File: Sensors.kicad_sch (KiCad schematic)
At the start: 3 parts, among them U2 ICM-42688-P, U3 BMP280, U4 INA226

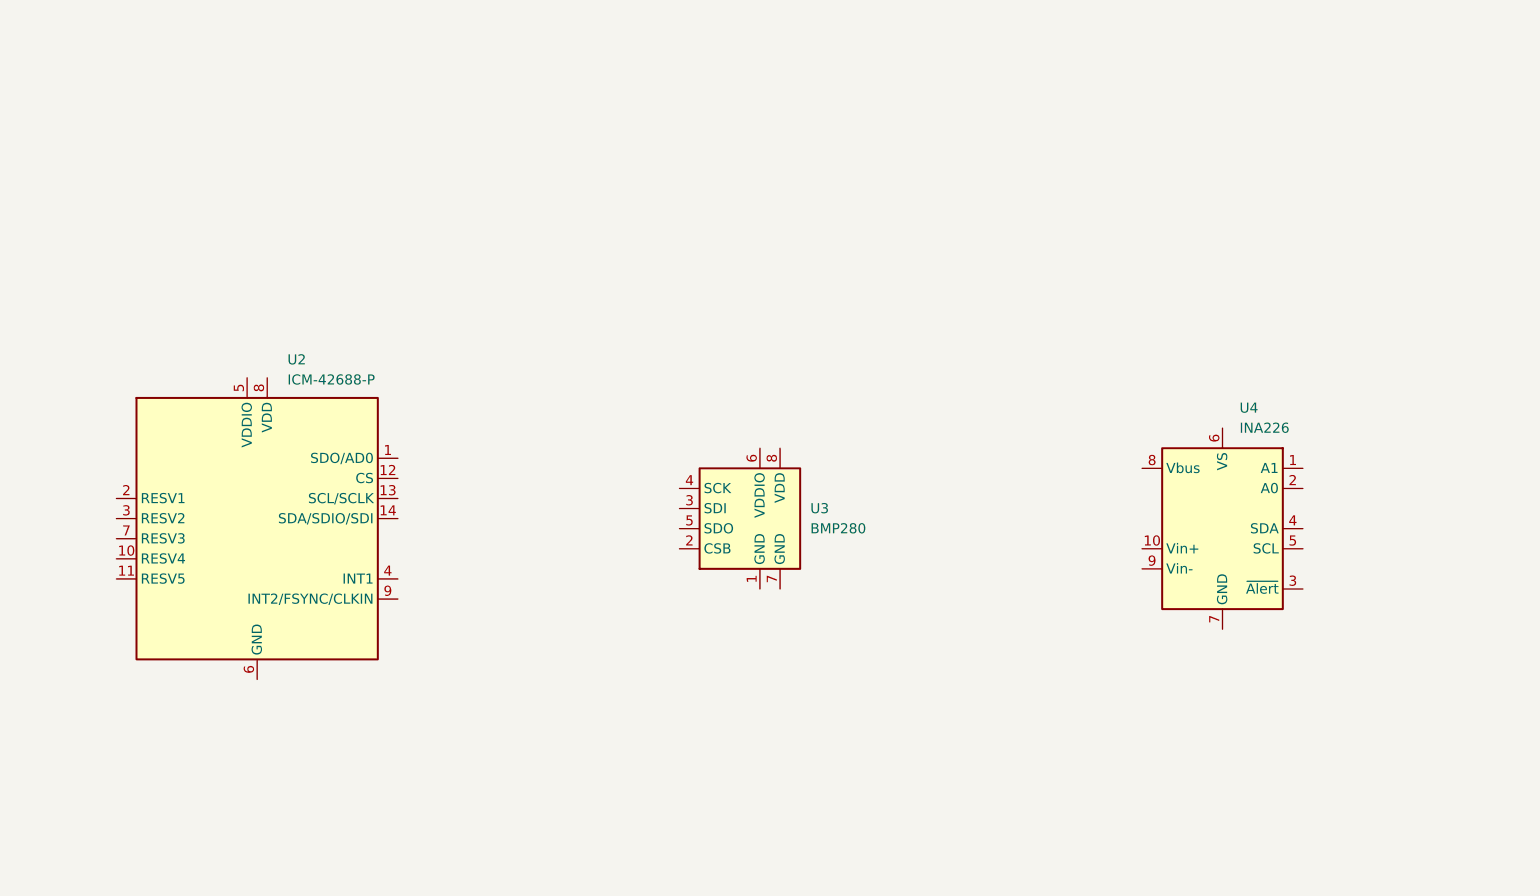
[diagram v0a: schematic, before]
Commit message: Sensors design
Updated the inertial measurement unit schematic.
Updated the power monitor schematic.
Updated the barometer schematic.
Updated the receiver schematic.

TODO:
Review the sensors schematic.
Implement ESC schematic.
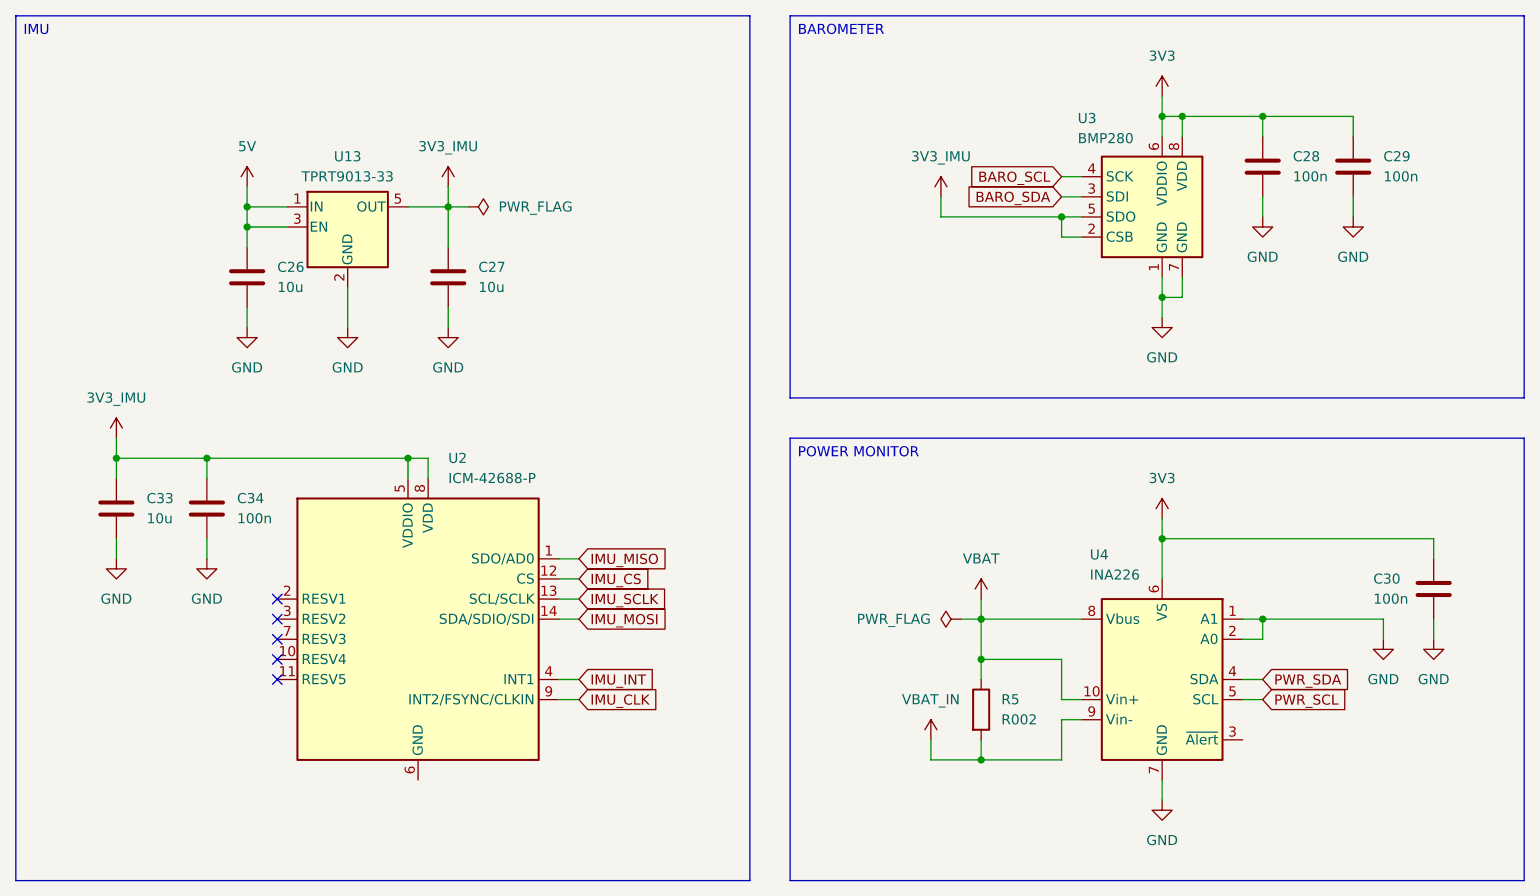
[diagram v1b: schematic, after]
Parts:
- added C26, C27, C33: 10u, symbol Device:C
- added C28, C29, C30, C34: 100n, symbol Device:C
- added R5: R002, symbol Device:R
- added U13: TPRT9013-33, Package_TO_SOT_SMD:SOT-23-5, symbol Regulator_Linear:TLV70233_SOT23-5
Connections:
- net GND: now reaches U4.1 (A1)
- net GND: now also U3.1 (GND), U3.7 (GND), U4.2 (A0), U4.7 (GND), C26.2, C27.2, C28.2, C29.2, C30.2, C33.2, C34.2, U13.2 (GND)
- net VBAT: now reaches U4.10 (Vin+)
- net VBAT: now also U4.8 (Vbus), R5.1
- net PWR_SDA: now reaches U4.4 (SDA)
- net PWR_SCL: now reaches U4.5 (SCL)
- net 3V3: now reaches U4.6 (VS)
- net 3V3: now also U3.6 (VDDIO), U3.8 (VDD), C28.1, C29.1, C30.1
- net VBAT_IN: now reaches U4.9 (Vin-)
- net VBAT_IN: now also R5.2
- net 3V3_IMU: now reaches U3.2 (CSB)
- net 3V3_IMU: now also U2.5 (VDDIO), U2.8 (VDD), U3.5 (SDO), C27.1, C33.1, C34.1, U13.5 (OUT)
- net BARO_SDA: now reaches U3.3 (SDI)
- net BARO_SCL: now reaches U3.4 (SCK)
- net IMU_MISO: now reaches U2.1 (SDO/AD0)
- net IMU_CS: now reaches U2.12 (CS)
- net IMU_SCLK: now reaches U2.13 (SCL/SCLK)
- net IMU_MOSI: now reaches U2.14 (SDA/SDIO/SDI)
- net IMU_INT: now reaches U2.4 (INT1)
- net IMU_CLK: now reaches U2.9 (INT2/FSYNC/CLKIN)
- new net 5V: C26.1, U13.1 (IN), U13.3 (EN)
- no-connect marks 0 -> 5
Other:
- moved on the sheet: U2, U3, U4

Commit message: ESC design
Updated the ESC schematic.
Replaces the INA 226 with INA230.
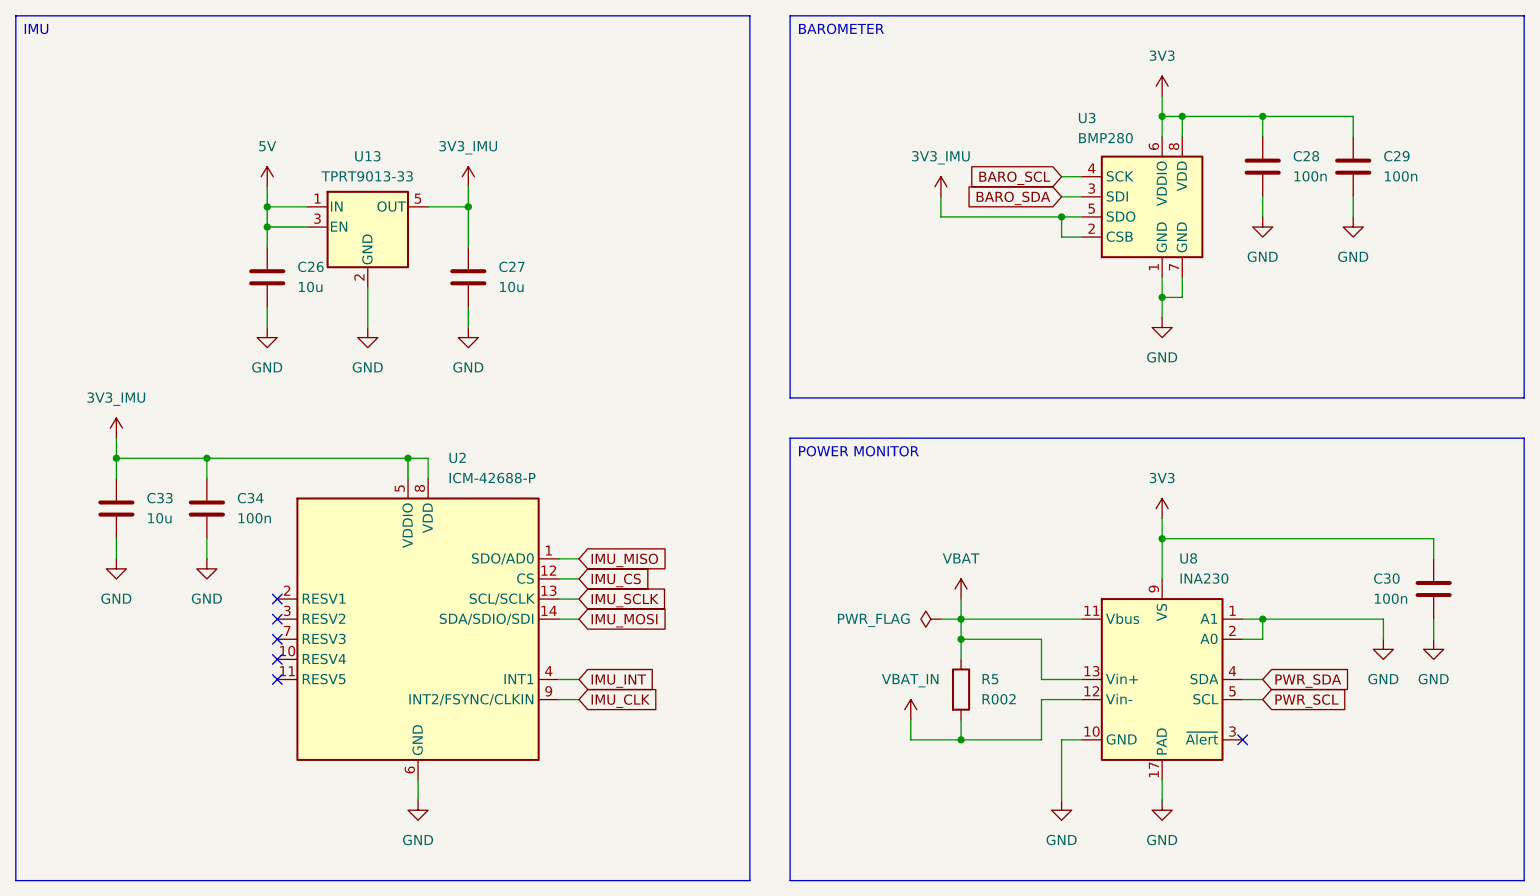
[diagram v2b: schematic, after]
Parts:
- removed U4: INA226, Package_SO:VSSOP-10_3x3mm_P0.5mm, symbol Sensor_Energy:INA226
- added U8: INA230, Custom_Parts:VQFN-16-1EP_3x3mm_P0.5mm_EP1.6x1.6mm_ThermalVias, symbol Custom_Parts:INA230
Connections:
- net 3V3: now also U8.9 (VS)
- net GND: now also U2.6 (GND), U8.1 (A1), U8.10 (GND), U8.17 (PAD), U8.2 (A0)
- net PWR_SCL: now also U8.5 (SCL)
- net PWR_SDA: now also U8.4 (SDA)
- net VBAT: now also U8.11 (Vbus), U8.13 (Vin+)
- net VBAT_IN: now also U8.12 (Vin-)
- no-connect marks 5 -> 6
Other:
- moved on the sheet: C26, C27, R5, U13

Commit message: MCU design
Updated the main RP2350 schematic.
Updated labels for other designs.
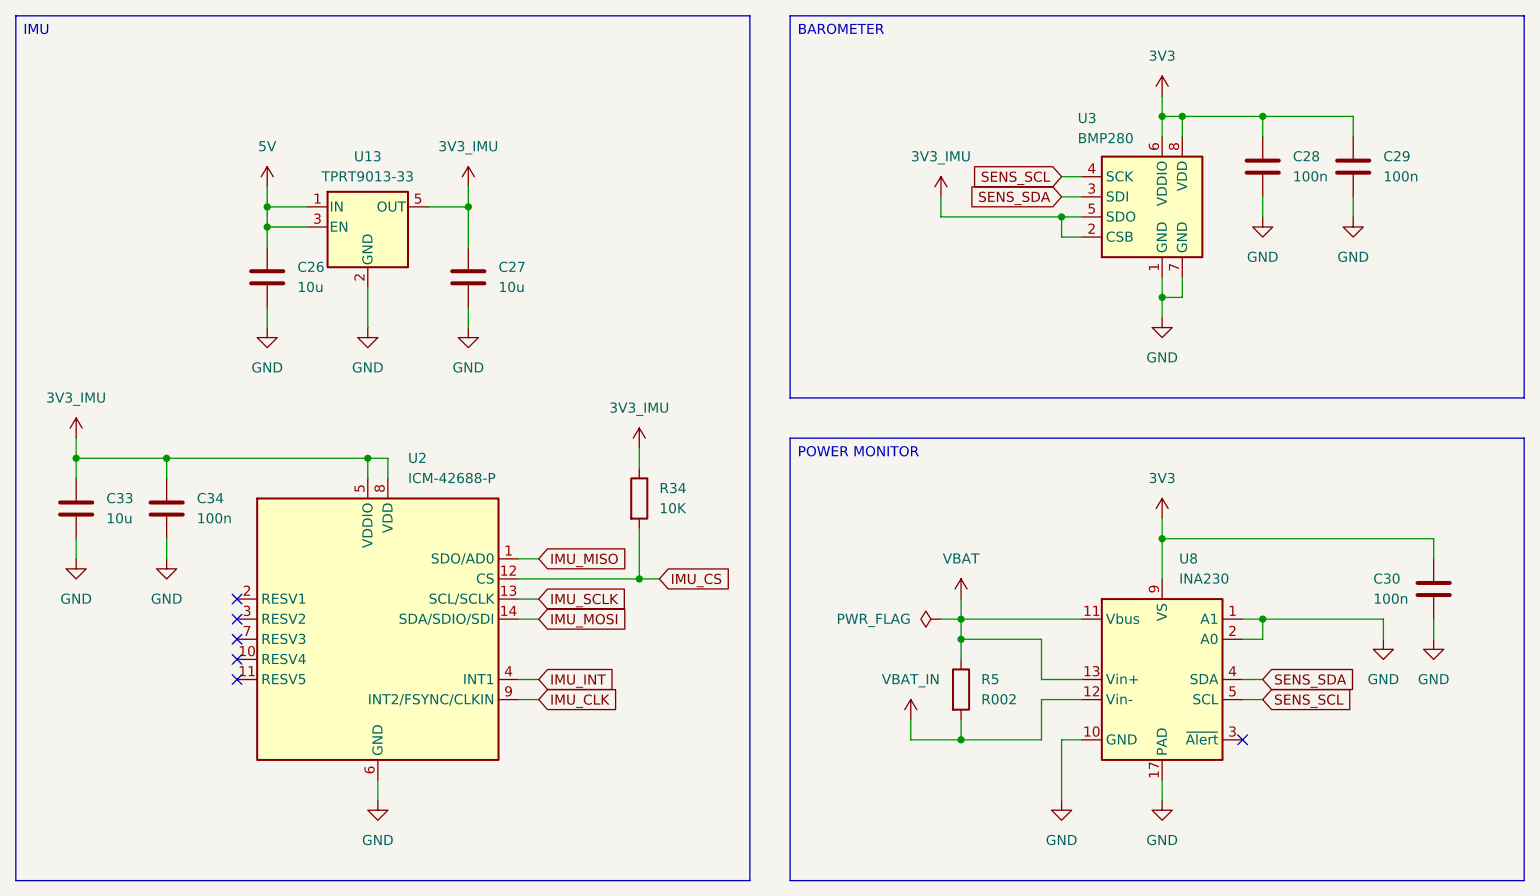
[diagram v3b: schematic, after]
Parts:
- added R34: 10K, symbol Device:R
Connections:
- net PWR_SCL is gone; now on net SENS_SCL: U8.5 (SCL)
- net PWR_SDA is gone; now on net SENS_SDA: U8.4 (SDA)
- net 3V3_IMU: now also R34.1
- net IMU_CS: now also R34.2
- net BARO_SCL renamed SENS_SCL
- net BARO_SDA renamed SENS_SDA
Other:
- moved on the sheet: C33, C34, U2

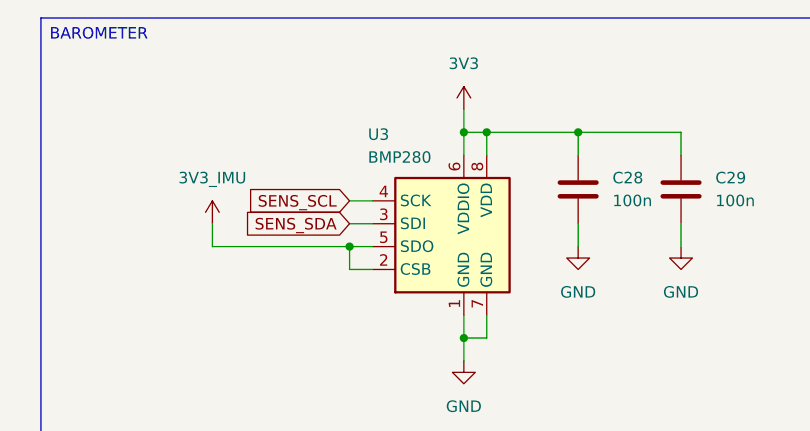
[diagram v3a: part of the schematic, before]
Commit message: Power design
Added the 5V regulator schematic.
Updated the MCU schematic.
Updated the RX schematic.
Updated the sensors schematic.

TODO:
Calculate the voltage divider for the 5V regulator.
Review all connections and systems.
Select the footprints for the missing components.
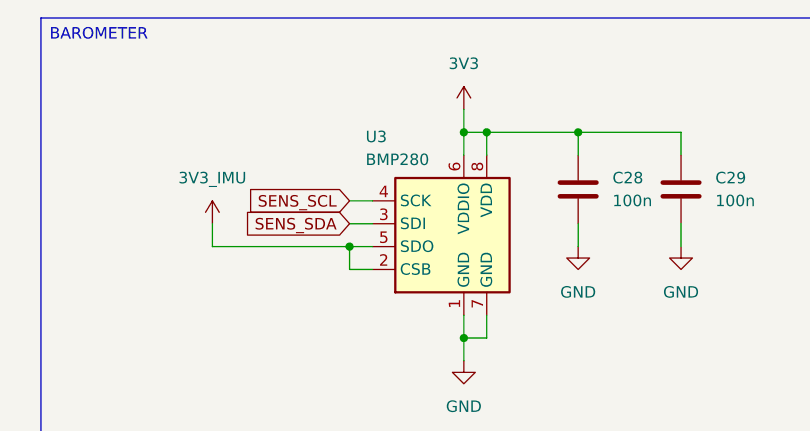
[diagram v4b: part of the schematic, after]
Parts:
- removed U3: BMP280, Package_LGA:Bosch_LGA-8_2x2.5mm_P0.65mm_ClockwisePinNumbering, symbol Sensor_Pressure:BMP280
- added U3: BMP280, Package_LGA:Bosch_LGA-8_2x2.5mm_P0.65mm_ClockwisePinNumbering, symbol Custom_Parts:BMP280
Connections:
- net 3V3: now also U3.6 (VDDIO), U3.8 (VDD)
- net 3V3_IMU: now also U3.2 (CSB), U3.5 (SDO)
- net GND: now also U3.1 (GND), U3.7 (GND)
- net SENS_SCL: now also U3.4 (SCK)
- net SENS_SDA: now also U3.3 (SDI)
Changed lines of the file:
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@@
+	)
+	(symbol
+		(lib_id "Custom_Parts:BMP280")
+		(at 198.12 64.77 0)
+		(unit 1)
+		(exclude_from_sim no)
+		(in_bom yes)
+		(on_board yes)
+		(dnp no)
+		(property "Reference" "U3"
+			(at 187.198 52.578 0)
+			(effects
+				(font
+					(size 1.27 1.27)
+				)
+				(justify left)
+			)
+		)
+		(property "Value" "BMP280"
+			(at 187.198 55.118 0)
+			(effects
+				(font
+					(size 1.27 1.27)
+				)
+				(justify left)
+			)
+		)
+		(property "Footprint" "Package_LGA:Bosch_LGA-8_2x2.5mm_P0.65mm_ClockwisePinNumbering"
+			(at 198.12 82.55 0)
+			(effects
+				(font
+					(size 1.27 1.27)
+				)
+				(hide yes)
+			)
+		)
+		(property "Datasheet" "https://ae-bst.resource.bosch.com/media/_tech/media/datasheets/BST-BMP280-DS001.pdf"
+			(at 198.12 64.77 0)
+			(effects
+				(font
+					(size 1.27 1.27)
+				)
+				(hide yes)
+			)
+		)
+		(property "Description" "Absolute Barometric Pressure Sensor, LGA-8"
+			(at 198.12 64.77 0)
+			(effects
+				(font
+					(size 1.27 1.27)
+				)
+				(hide yes)
+			)
+		)
+		(pin "4"
+		)
+		(pin "6"
+		)
+		(pin "3"
+		)
+		(pin "5"
+		)
+		(pin "2"
+		)
+		(pin "1"
+		)
+		(pin "8"
+		)
+		(pin "7"
+		)
+		(instances
+			(project ""
+				(path "/ac187c6c-fa53-41cc-bce1-6f39a42a92e8/593939c9-ca21-46a5-baaf-5c6ecc4a9199"
+					(reference "U3")
+					(unit 1)
+				)
+			)
+		)
 	)
 	(symbol
@@
 					(unit 1)
 				)
-			)
-		)
-	)
-	(symbol
-		(lib_id "Sensor_Pressure:BMP280")
-		(at 198.12 64.77 0)
-		(unit 1)
-		(exclude_from_sim no)
-		(in_bom yes)
-		(on_board yes)
-		(dnp no)
-		(property "Reference" "U3"
-			(at 187.452 52.324 0)
-			(effects
-				(font
-					(size 1.27 1.27)
-				)
-				(justify left)
-			)
-		)
-		(property "Value" "BMP280"
-			(at 187.452 54.864 0)
-			(effects
-				(font
-					(size 1.27 1.27)
-				)
-				(justify left)
-			)
-		)
-		(property "Footprint" "Package_LGA:Bosch_LGA-8_2x2.5mm_P0.65mm_ClockwisePinNumbering"
-			(at 198.12 82.55 0)
-			(effects
-				(font
-					(size 1.27 1.27)
-				)
-				(hide yes)
-			)
-		)
-		(property "Datasheet" "https://ae-bst.resource.bosch.com/media/_tech/media/datasheets/BST-BMP280-DS001.pdf"
-			(at 198.12 64.77 0)
-			(effects
-				(font
-					(size 1.27 1.27)
-				)
-				(hide yes)
-			)
-		)
-		(property "Description" "Absolute Barometric Pressure Sensor, LGA-8"
-			(at 198.12 64.77 0)
-			(effects
-				(font
-					(size 1.27 1.27)
-				)
-				(hide yes)
-			)
-		)
-		(pin "3"
-		)
-		(pin "2"
-		)
-		(pin "4"
-		)
-		(pin "8"
-		)
-		(pin "7"
-		)
-		(pin "6"
-		)
-		(pin "1"
-		)
-		(pin "5"
-		)
-		(instances
-			(project ""
-				(path "/ac187c6c-fa53-41cc-bce1-6f39a42a92e8/593939c9-ca21-46a5-baaf-5c6ecc4a9199"
-					(reference "U3")
-					(unit 1)
-				)
